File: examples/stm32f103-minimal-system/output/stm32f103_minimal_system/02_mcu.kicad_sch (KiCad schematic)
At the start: 7 parts, among them SW1 SW-TH_6x6, U1 STM32F103C8T6, Y1 8MHz

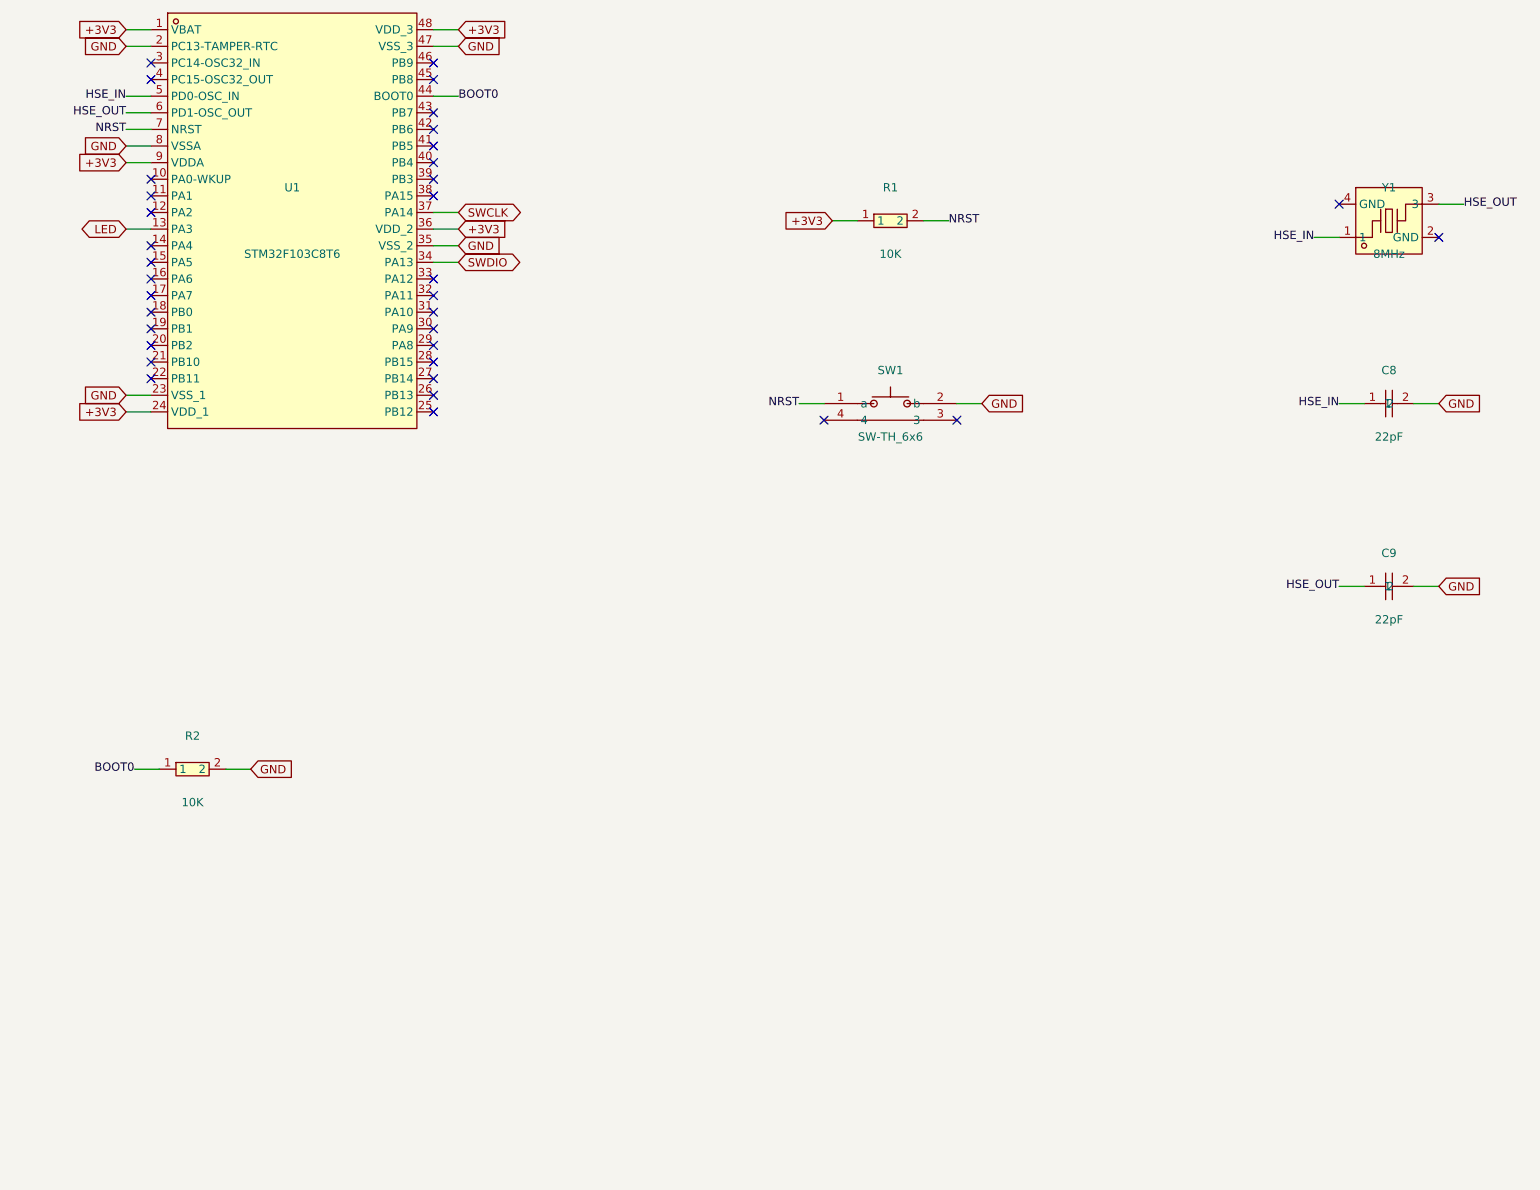
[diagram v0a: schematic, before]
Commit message: chore(example): update STM32F103 with easyeda2kicad symbols, footprints, and PCB layout 更新示例：easyeda2kicad 符号+封装、PCB 布局
- All symbols regenerated via easyeda2kicad (correct pin alignment)
- All footprints now have real pads from EasyEDA data
- Add pcb_layout.regions to circuit-model.json for agent-driven PCB placement
- Refresh schematics, reports, and operation logs from latest pipeline

Co-Authored-By: Claude Opus 4.7 <noreply@anthropic.com>
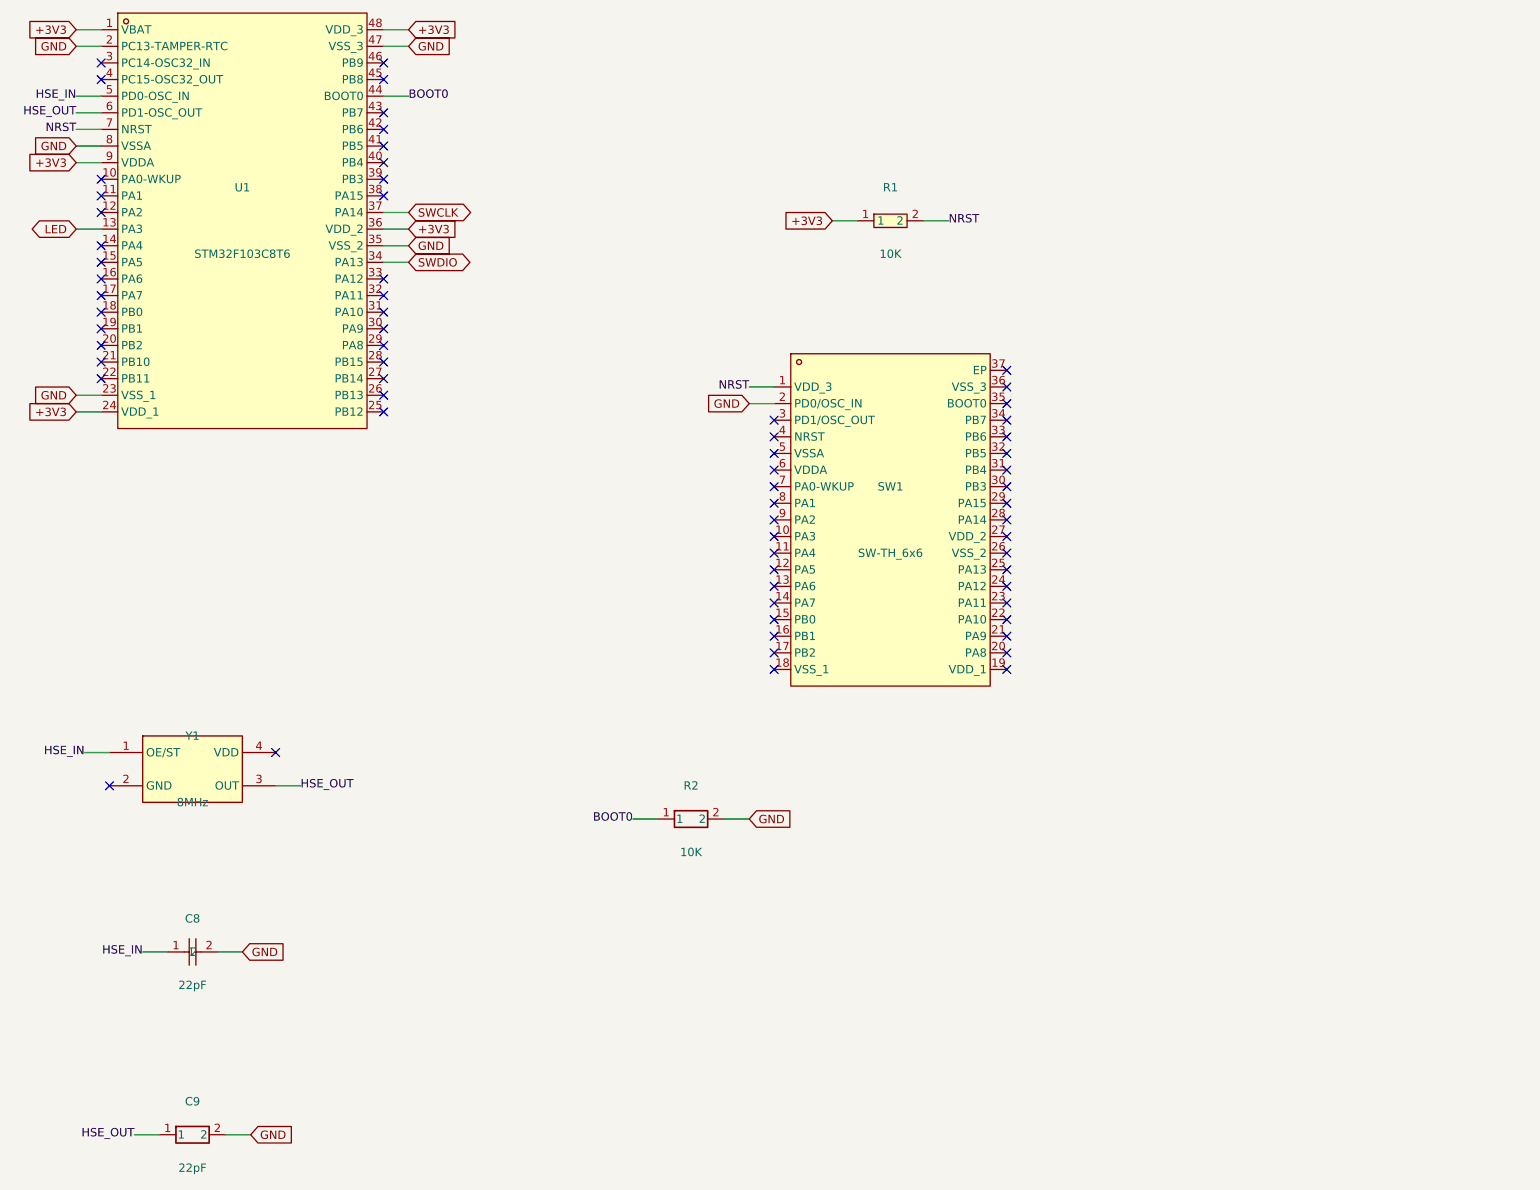
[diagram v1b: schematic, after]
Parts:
- removed C9: 22pF, symbol JLC-MCP:CL10C220JB8NNNC
- removed R2: 10K, symbol JLC-MCP:0603WAJ0103T5E
- removed SW1: SW-TH_6x6, symbol JLC-MCP:K5-1617SA-01
- removed Y1: 8MHz, symbol JLC-MCP:HY8MSMD3225OB1R30
- added C9: 22pF, symbol JLC-MCP:C1653
- added R2: 10K, symbol JLC-MCP:C15401
- added SW1: SW-TH_6x6, symbol JLC-MCP:STM32F103TBU6
- added Y1: 8MHz, symbol JLC-MCP:SiT8008AI-22-33E-8.000000D
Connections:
- net BOOT0: now also R2.1
- net GND: now also C9.2, R2.2, SW1.2 (PD0/OSC_IN)
- net HSE_IN: now also Y1.1 (OE/ST)
- net HSE_OUT: now also C9.1, Y1.3 (OUT)
- net NRST: now also SW1.1 (VDD_3)
- no-connect marks 35 -> 68
